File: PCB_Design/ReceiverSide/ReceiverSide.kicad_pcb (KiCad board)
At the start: 2 copper layers, 15 parts, among them J1 Conn_01x02_Pin, U1 DRV5053CAQLPGM

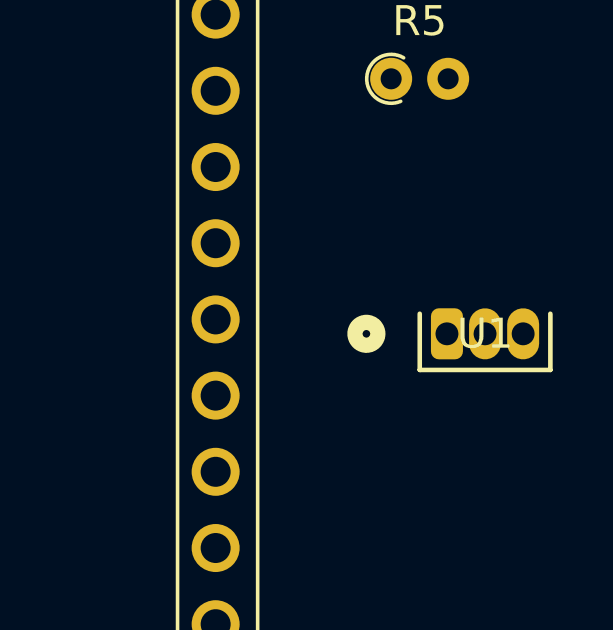
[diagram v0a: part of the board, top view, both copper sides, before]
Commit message: Transmitter PCB temp layout
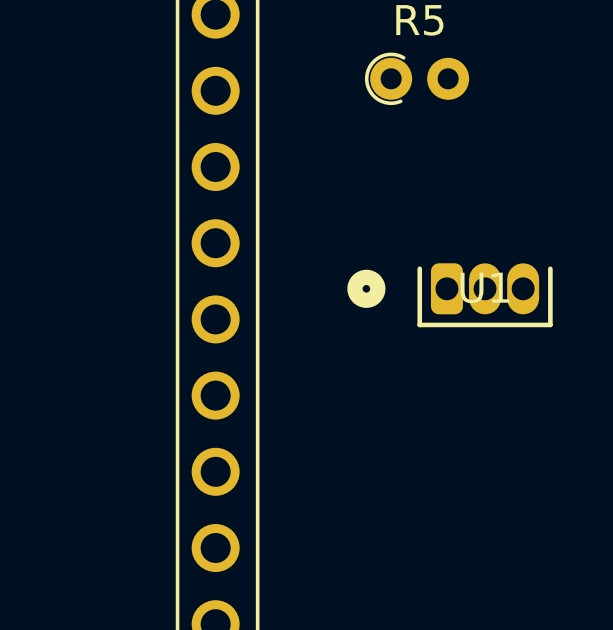
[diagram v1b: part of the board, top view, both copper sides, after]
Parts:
- moved U1 1.50 mm to (147.0, 72.5)
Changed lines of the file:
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@@
 	(footprint "Halleffect:LPG3_TEX"
 		(layer "F.Cu")
-		(at 146.96 74)
+		(at 146.96 72.5)
 		(tags "DRV5053CAQLPGM ")
 		(property "Reference" "U1"

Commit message: COMPLETED RECIVER PCB
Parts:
- removed J1: Conn_01x02_Pin, Connector_PinHeader_1.27mm:PinHeader_1x02_P1.27mm_Vertical
- removed LS1: Speaker, Resistor_THT:R_Axial_DIN0204_L3.6mm_D1.6mm_P1.90mm_Vertical
- removed R6: R, Resistor_THT:R_Axial_DIN0204_L3.6mm_D1.6mm_P1.90mm_Vertical
- removed R9: R_Photo, Resistor_THT:R_Axial_DIN0204_L3.6mm_D1.6mm_P1.90mm_Vertical
- removed U1: DRV5053CAQLPGM, Halleffect:LPG3_TEX
- added ACC1: R, Resistor_THT:R_Axial_DIN0204_L3.6mm_D1.6mm_P5.08mm_Horizontal, F.Cu at (168.0, 102.8)
- added ACC2: R, Resistor_THT:R_Axial_DIN0204_L3.6mm_D1.6mm_P5.08mm_Horizontal, F.Cu at (168.0, 97.8)
- added ACC3: R, Resistor_THT:R_Axial_DIN0204_L3.6mm_D1.6mm_P5.08mm_Horizontal, F.Cu at (178.4, 81.8)
- added ACC4: R, Resistor_THT:R_Axial_DIN0204_L3.6mm_D1.6mm_P5.08mm_Horizontal, F.Cu at (180.9, 76.7)
- added ACC5: R, Resistor_THT:R_Axial_DIN0204_L3.6mm_D1.6mm_P5.08mm_Horizontal, F.Cu at (186.8, 88.8)
- added AUX-PWR1: Conn_01x02_Socket, Connector_PinSocket_2.54mm:PinSocket_1x02_P2.54mm_Vertical, F.Cu at (165.5, 113.8)
- added H1: MountingHole, MountingHole:MountingHole_2.7mm, F.Cu at (125.2, 66.2)
- added H2: MountingHole, MountingHole:MountingHole_2.7mm, F.Cu at (125.2, 115.5)
- added H3: MountingHole, MountingHole:MountingHole_2.7mm, F.Cu at (186.5, 115.5)
- added H4: MountingHole, MountingHole:MountingHole_2.7mm, F.Cu at (186.5, 66.2)
- added HALL-IN1: Conn_01x01_Socket, Connector_PinSocket_2.54mm:PinSocket_1x01_P2.54mm_Vertical, F.Cu at (163.5, 91.2)
- added Hall1: Conn_01x02_Socket, Connector_PinSocket_2.54mm:PinSocket_1x02_P2.54mm_Vertical, F.Cu at (163.5, 81.8)
- added OP-IN1: Conn_01x02_Socket, Connector_PinSocket_2.54mm:PinSocket_1x02_P2.54mm_Vertical, F.Cu at (180.9, 70.8)
- added OP-OUT1: Conn_01x01_Socket, Connector_PinSocket_2.54mm:PinSocket_1x01_P2.54mm_Vertical, F.Cu at (177.9, 99.5)
- added OP-PWR1: Conn_01x02_Socket, Connector_PinSocket_2.54mm:PinSocket_1x02_P2.54mm_Vertical, F.Cu at (173.5, 113.7)
- added Op-Amp1: MCP6281-E_P, MCP6281_E_P:DIP787W46P254L927H533Q8, F.Cu at (179.6, 90.5)
- added PR1: R_Photo, Resistor_THT:R_Axial_DIN0204_L3.6mm_D1.6mm_P5.08mm_Horizontal, F.Cu at (162.5, 74.0)
- added Speaker1: Conn_01x02_Socket, Connector_PinSocket_2.54mm:PinSocket_1x02_P2.54mm_Vertical, F.Cu at (135.5, 107.5)
- R1, R2, R3, R4, R5: footprint Resistor_THT:R_Axial_DIN0204_L3.6mm_D1.6mm_P1.90mm_Vertical -> Resistor_THT:R_Axial_DIN0204_L3.6mm_D1.6mm_P5.08mm_Horizontal
- moved A1 27.0 mm to (142.5, 75.4)
- moved R1 26.3 mm to (136.3, 77.5), turned to 180 degrees
- moved R3 24.8 mm to (136.3, 90.8), turned to 180 degrees
- moved R2 24.6 mm to (136.3, 84.0), turned to 180 degrees
- moved R4 23.3 mm to (136.3, 96.0), turned to 180 degrees
- moved D2 20.2 mm to (124.5, 83.8), turned to 0 degrees
- moved D3 20.0 mm to (124.5, 91.0), turned to 0 degrees
- moved D1 19.8 mm to (124.5, 75.8), turned to 0 degrees
- moved D4 19.8 mm to (124.5, 98.2), turned to 0 degrees
- moved R5 18.0 mm to (162.5, 70.2)
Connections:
- A1 pad 9: /D6 -> /Speaker
- D1 pad 1: /LEDa -> GND
- D1 pad 2: GND -> Net-(D1-A)
- D2 pad 1: /LEDb -> GND
- D2 pad 2: GND -> Net-(D2-A)
- D3 pad 1: /LEDc -> GND
- D3 pad 2: GND -> Net-(D3-A)
- D4 pad 1: /LEDd -> GND
- D4 pad 2: GND -> Net-(D4-A)
- R1 pad 2: /LEDa -> Net-(D1-A)
- R2 pad 2: /LEDb -> Net-(D2-A)
- R3 pad 2: /LEDc -> Net-(D3-A)
- R4 pad 2: /LEDd -> Net-(D4-A)
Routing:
- net Net-(A1-VIN): track 0.00 -> 47.0 mm
- net /VSS-: track 0.00 -> 28.1 mm
- net /Photores: track 0.00 -> 24.5 mm
- net /VDD+: track 0.00 -> 21.6 mm
- net +5V: track 0.00 -> 16.3 mm
- net /VOUT: track 0.00 -> 16.0 mm
- net /Speaker: track 0.00 -> 14.6 mm
- net /LED1: track 0.00 -> 10.7 mm
- net Net-(Op-Amp1-VIN-): track 0.00 -> 10.7 mm
- net /LED2: track 0.00 -> 7.90 mm
- net /LED4: track 0.00 -> 7.55 mm
- net /Halleffect: track 0.00 -> 7.07 mm
- net /LED3: track 0.00 -> 6.53 mm
- net Net-(OP-IN1-Pin_2): track 0.00 -> 5.93 mm
- net Net-(OP-IN1-Pin_1): track 0.00 -> 5.93 mm
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- added copper zone on B.Cu, net GND
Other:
- board outline added: 69 x 57 mm
- board text added: "+"
- board text added: "-"
- board text added: "GND"
- board text added: "VDD-"
- board text added: "VSS-"

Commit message: PCB DONE
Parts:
- added GND1: Conn_01x01_Socket, Connector_PinSocket_2.54mm:PinSocket_1x01_P2.54mm_Vertical, F.Cu at (173.0, 79.2)
- added GND2: Conn_01x01_Socket, Connector_PinSocket_2.54mm:PinSocket_1x01_P2.54mm_Vertical, F.Cu at (173.0, 73.2)
- added OP-PWR-IN1: Conn_01x02_Socket, Connector_PinSocket_2.54mm:PinSocket_1x02_P2.54mm_Vertical, F.Cu at (153.0, 68.8)
- moved H1 5.77 mm to (124.8, 60.5)
- moved H4 5.75 mm to (186.5, 60.5)
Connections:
- A1 pad 17: unconnected-(A1-3V3-Pad17) -> +3.3V
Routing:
- net +3.3V: track 0.00 -> 81.4 mm
- net +5V: track 16.3 -> 29.1 mm
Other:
- board size 69 x 57 mm -> 70.5 x 65 mm
